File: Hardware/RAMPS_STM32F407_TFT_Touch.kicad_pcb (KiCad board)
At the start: 2 copper layers, 110 x 83.7 mm, 99 parts, among them J1 TEMP_0, J10 FAN2, J11 FAN1, J12 X_logic, J13 Microsteps, J14 X-, J15 Y-, J16 Z-, J17 Left, J18 Y_logic, J19 X+, J2 TEMP_1, J20 Y+, J21 Z+, J22 Microsteps, J23 LCD2, J24 Z_logic, J25 TFT_FSCM, J26 Microsteps, J27 LCD1, J28 E0_logic, J29 Microsteps, J3 TEMP_B, J30 Right, J31 E1_logic, J32 Microsteps, J33 X_motor, J34 Y_motor, J35 Z_motor, J36 E0_motor, J37 E1_motor, J38 X, J39 Y, J4 TEMP_C, J40 Z, J41 E0, J42 E1, J43 FAN0, J44 COM, J45 USB, J46 Power, J47 I2C, J48 SPI, J49 SPI, J5 -VIN+, J50 SDIO, J51 Servo, J52 Servo, J53 PowerSelect, J54 Power, J56 Power, J6 HEATER_B, J7 HEATER_0, J8 HEATER_1, J9 FAN3, Q1 NTMFS5C628, Q2 NTMFS5C628, Q3 NTMFS5C628, Q4 BUK9K17-60E, Q5 BUK9K17-60E, U1 74LVC125, X01 MP2315, X02 MP2315

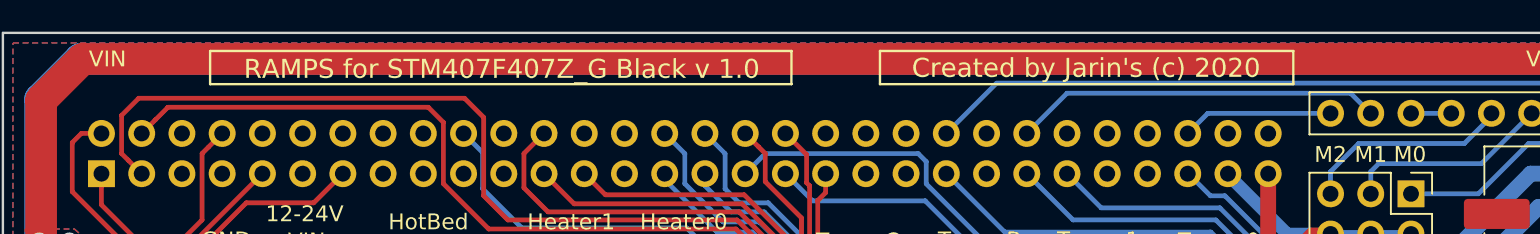
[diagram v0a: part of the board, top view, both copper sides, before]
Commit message: Added KiCADlibrary and 3Dshapes
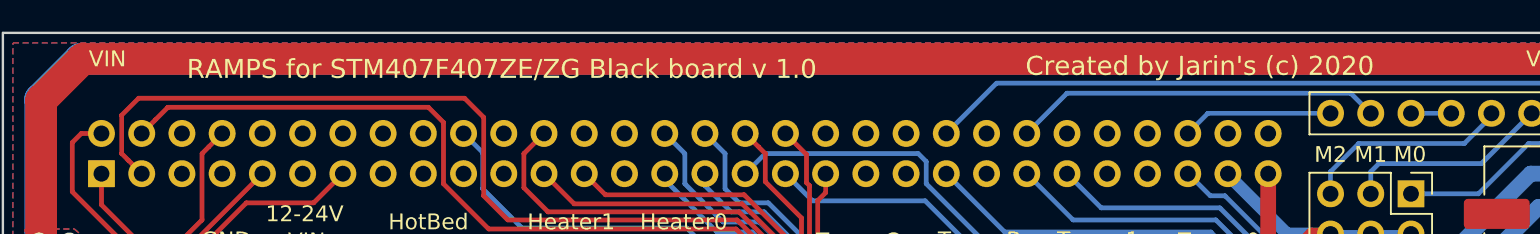
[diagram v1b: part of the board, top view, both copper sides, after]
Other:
- board text added: "RAMPS for STM407F407ZE/ZG Black board v 1.0"
- board text removed: "RAMPS for STM407F407Z_G Black v 1.0"
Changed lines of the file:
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@@
   (general
     (thickness 1.6)
-    (drawings 236)
+    (drawings 228)
     (tracks 1220)
     (zones 0)
@@
     (34 B.Paste user hide)
     (35 F.Paste user hide)
-    (36 B.SilkS user hide)
-    (37 F.SilkS user)
+    (36 B.SilkS user)
+    (37 F.SilkS user hide)
     (38 B.Mask user hide)
     (39 F.Mask user hide)
@@
   )
   (setup
-    (last_trace_width 1)
+    (last_trace_width 0.3)
     (user_trace_width 0.3)
     (user_trace_width 0.35)
@@
     (effects (font (size 0.8 0.8) (thickness 0.15)) (justify mirror))
   )
-  (gr_line (start 81.4705 1.143) (end 55.372 1.143) (layer F.SilkS) (width 0.15))
-  (gr_line (start 55.372 3.2385) (end 81.4705 3.2385) (layer F.SilkS) (width 0.15))
-  (gr_line (start 81.4705 3.2385) (end 81.4705 1.143) (layer F.SilkS) (width 0.15))
-  (gr_line (start 55.372 1.143) (end 55.372 3.2385) (layer F.SilkS) (width 0.15))
-  (gr_line (start 13.081 3.2385) (end 49.784 3.2385) (layer F.SilkS) (width 0.15))
-  (gr_line (start 13.081 1.143) (end 13.081 3.2385) (layer F.SilkS) (width 0.15))
-  (gr_line (start 49.784 1.143) (end 13.081 1.143) (layer F.SilkS) (width 0.15))
-  (gr_line (start 49.784 3.2385) (end 49.784 1.143) (layer F.SilkS) (width 0.15))
   (gr_text "Power supply for \nexternal use" (at 38.9255 52.578) (layer F.SilkS)
     (effects (font (size 0.8 0.8) (thickness 0.12)))
@@
     (effects (font (size 1 1) (thickness 0.15)))
   )
-  (gr_text "Created by Jarin's (c) 2020" (at 68.3895 2.2225) (layer F.SilkS)
+  (gr_text "Created by Jarin's (c) 2020" (at 75.565 2.0955) (layer F.SilkS)
     (effects (font (size 1.2 1.2) (thickness 0.15)))
   )
-  (gr_text "RAMPS for STM407F407Z_G Black v 1.0" (at 31.496 2.286) (layer F.SilkS)
+  (gr_text "RAMPS for STM407F407ZE/ZG Black board v 1.0" (at 31.496 2.286) (layer F.SilkS)
     (effects (font (size 1.2 1.2) (thickness 0.15)))
   )
@@
     (effects (font (size 1 1) (thickness 0.15)) (justify mirror))
   )
-  (gr_text "Created by Jarin's (c) 2020" (at 19.4945 71.12) (layer B.SilkS)
+  (gr_text "Created by Jarin's (c) 2020" (at 14.2875 71.5645) (layer B.SilkS)
     (effects (font (size 1.2 1.2) (thickness 0.15)) (justify mirror))
   )
-  (gr_text "RAMPS for STM407F407Z_G Black v 1.0" (at 20.193 68.834) (layer B.SilkS)
+  (gr_text "RAMPS for STM407F407ZE/ZG Black board v 1.0" (at 23.8125 69.1515) (layer B.SilkS)
     (effects (font (size 1.2 1.2) (thickness 0.15)) (justify mirror))
   )
@@
   (gr_poly (pts (xy 136.5 115.6) (xy 142.9 115.6) (xy 142.9 121.4) (xy 136.5 121.4)) (layer B.Mask) (width 0.15))
   (gr_poly (pts (xy 136.525 113.665) (xy 136.525 102.87) (xy 146.05 102.87) (xy 146.05 113.665)) (layer B.Mask) (width 0.15))
-  (via (at 40.386 68.8975) (size 0.8) (drill 0.4) (layers F.Cu B.Cu) (net 7))
   (segment (start 47.839 61.8725) (end 46.228 61.8725) (width 1.5) (layer F.Cu) (net 1))
   (segment (start 49.4665 68.8975) (end 49.4665 63.5) (width 1.5) (layer F.Cu) (net 1))
@@
   (segment (start 34.5865 34.5625) (end 34.5865 28.088) (width 0.3) (layer F.Cu) (net 6))
   (segment (start 34.5865 28.088) (end 35.179 27.4955) (width 0.3) (layer F.Cu) (net 6))
+  (via (at 40.386 68.8975) (size 0.8) (drill 0.4) (layers F.Cu B.Cu) (net 7))
   (segment (start 28.0975 68.9025) (end 27.813 68.618) (width 0.3) (layer F.Cu) (net 7))
   (segment (start 27.846 68.9025) (end 27.813 68.9355) (width 0.5) (layer F.Cu) (net 7))

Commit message: Add Gerber files
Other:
- board text added: "VIN - 24V"
- board text removed: "CS1"
- board text removed: "CS2"

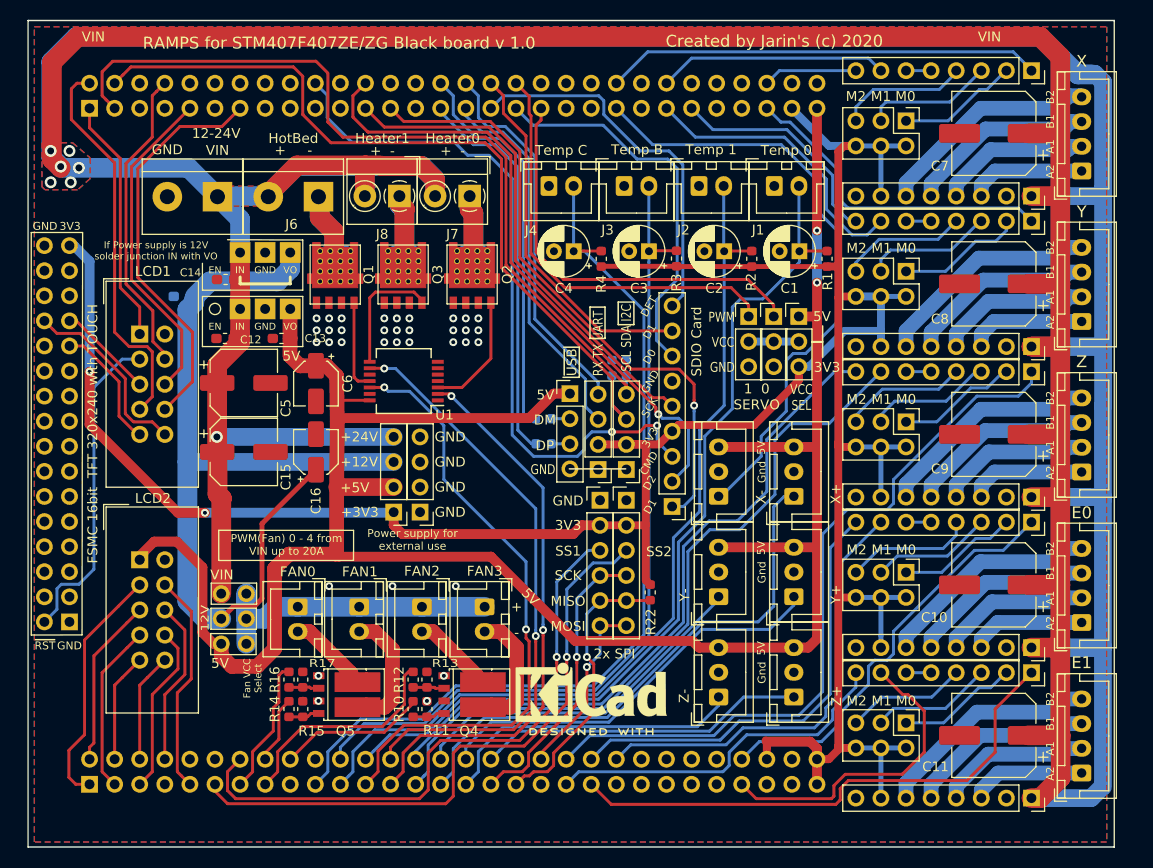
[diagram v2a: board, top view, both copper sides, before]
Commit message: Add fuse
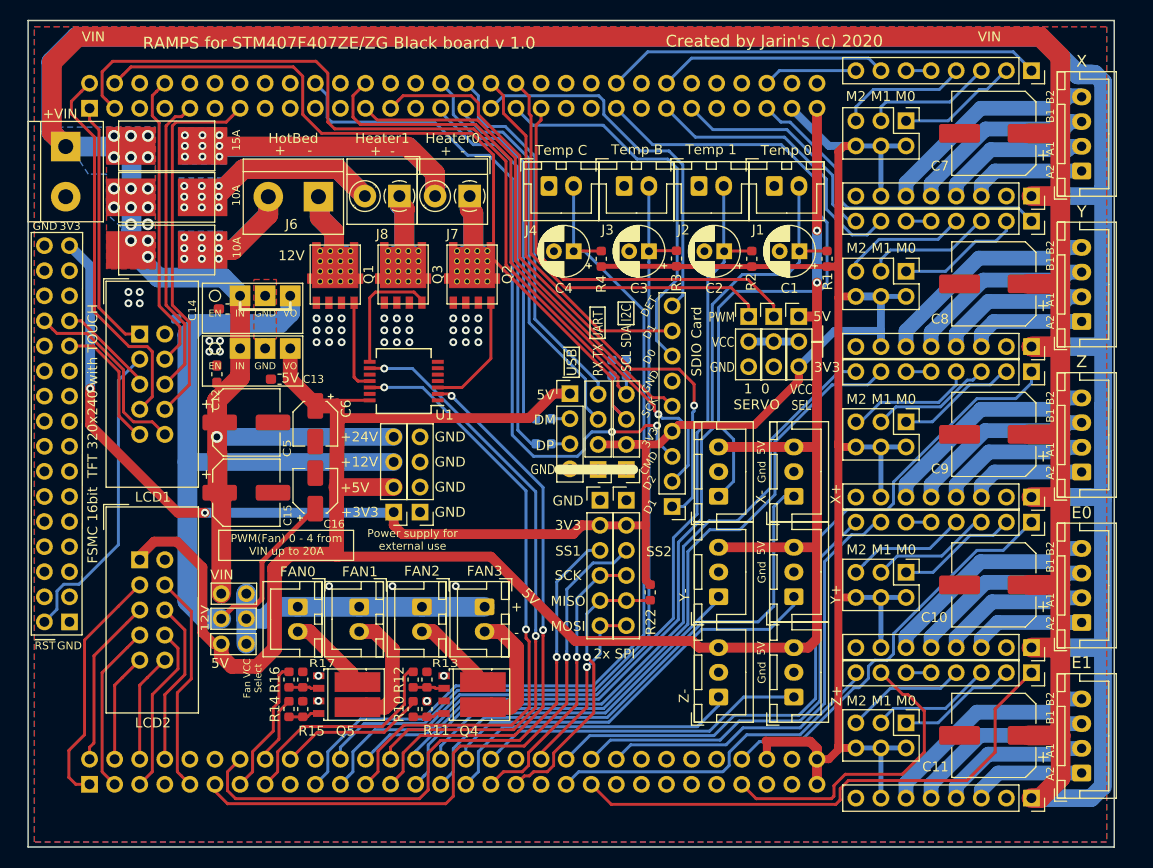
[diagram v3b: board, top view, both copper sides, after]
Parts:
- removed REF**: KiCad-Logo2_6mm_SilkScreen, Symbol:KiCad-Logo2_6mm_SilkScreen
- removed REF**: KiCad-Logo2_8mm_SilkScreen, Symbol:KiCad-Logo2_8mm_SilkScreen
- added F1: 15A, Jarin's:2410_FuseFolder, F.Cu at (14.0, 12.7)
- added F2: 10A, Jarin's:2410_FuseFolder, F.Cu at (14.0, 17.9)
- added F3: 10A, Jarin's:2410_FuseFolder, F.Cu at (14.0, 23.2)
- moved J5 16.2 mm to (3.81, 12.8), turned to 270 degrees
- moved X02 4.38 mm to (21.5, 27.9)
- moved C15 4.14 mm to (22.1, 47.8)
- moved C13 4.13 mm to (25.5, 36.3)
- moved C6 4.06 mm to (29.1, 40.8)
- moved C5 4.01 mm to (22.1, 40.7)
- moved X01 4.00 mm to (21.5, 33.2)
- moved C16 3.94 mm to (29.1, 47.6)
- moved C12 3.71 mm to (19.1, 35.8), turned to 90 degrees
- moved C14 2.99 mm to (20.2, 29.2)
- moved C17 2.30 mm to (15.9, 30.2)
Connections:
- J6 pad 2: +24V -> Net-(F3-Pad2)
- J7 pad 2: +24V -> Net-(F1-Pad2)
- J8 pad 2: +24V -> Net-(F2-Pad2)
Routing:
- net Net-(F1-Pad2): track 0.00 -> 53.0 mm, vias 0 -> 9
- net +24V: track 604.0 -> 553.2 mm, vias 7 -> 18
- net Net-(F2-Pad2): track 0.00 -> 36.4 mm, vias 0 -> 9
- net Net-(F3-Pad2): track 0.00 -> 19.9 mm, vias 0 -> 9
- net +12V: track 88.8 -> 81.4 mm
- net /X_MIN: track 62.1 -> 66.6 mm
- net +5V: track 232.4 -> 229.1 mm
- net /EN1: track 40.7 -> 38.0 mm
- net /EN2: track 33.2 -> 30.9 mm
- net /SDIO_D2: track 62.6 -> 64.0 mm
- net /TEMP_0: track 90.7 -> 92.0 mm
- net /~RESET: track 32.7 -> 31.5 mm
- net /E0_EN: track 42.3 -> 41.2 mm
- net /E1_DIR: track 36.2 -> 35.2 mm
- net /HEATER_B: track 62.3 -> 63.3 mm
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- added copper zone on B.Cu, net Net-(F1-Pad2)
- added copper zone on B.Cu, net Net-(F2-Pad2)
- added copper zone on B.Cu, net Net-(F3-Pad2)
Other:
- board text added: "+VIN"
- board text removed: "12-24V"
- board text removed: "If Power supply is 12V solder junction IN with VO"

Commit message: Add Schottky to 5V(usb port protection)
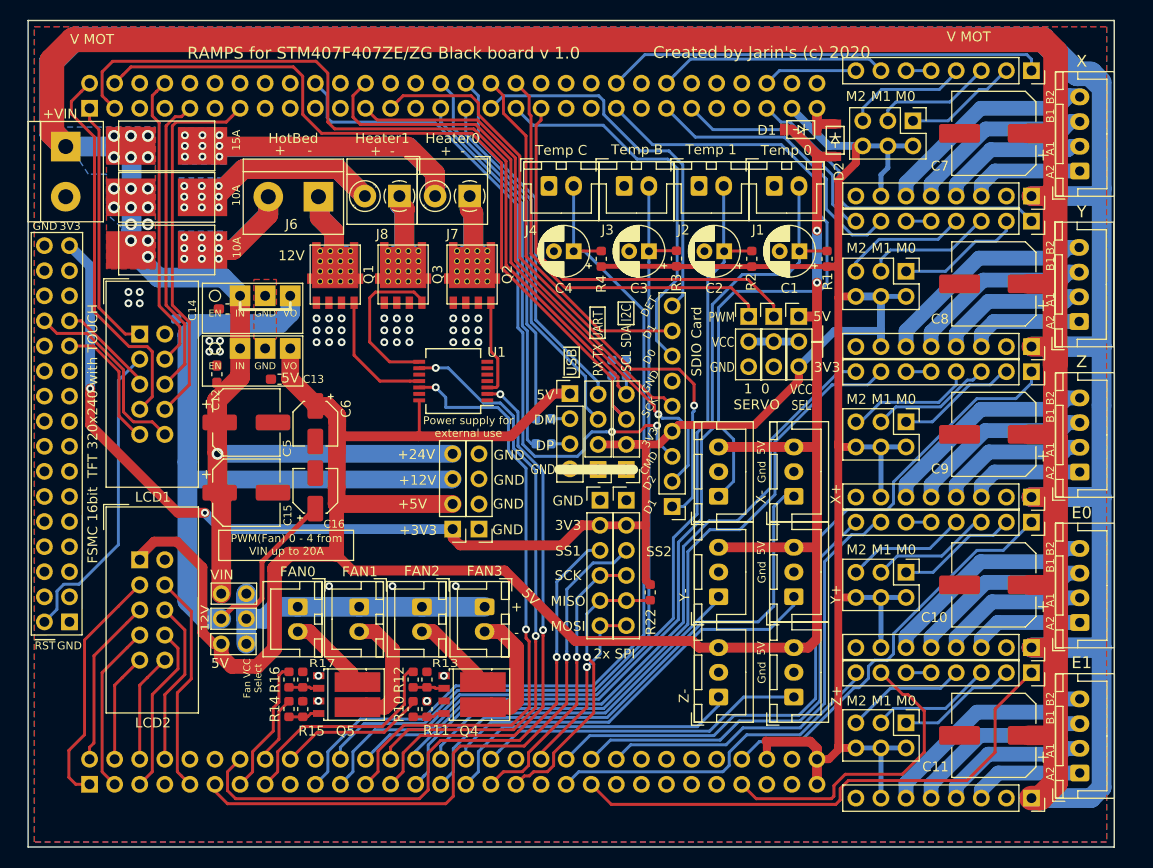
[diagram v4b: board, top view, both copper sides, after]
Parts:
- added D1: MBR130LSFT1G, Jarin's:D_SOD-123, F.Cu at (78.2, 11.0)
- added D2: MBR130LSFT1G, Jarin's:D_SOD-123, F.Cu at (81.7, 12.1)
- moved J46 6.21 mm to (45.7, 51.5)
- moved J54 6.21 mm to (43.0, 51.5)
- moved U1 5.02 mm to (43.1, 36.5)
- moved J13 0.70 mm to (89.6, 10.2)
- moved J39 0.25 mm to (106.4, 30.5)
- moved J38 0.19 mm to (106.5, 15.2)
- moved J40 0.19 mm to (106.5, 45.7)
- moved J41 0.19 mm to (106.5, 61.0)
- moved J42 0.19 mm to (106.5, 76.2)
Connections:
- J17 pad 59: +5V -> Net-(D1-Pad1)
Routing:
- net +5V: track 229.1 -> 238.5 mm
- net +12V: track 81.4 -> 89.2 mm
- net Net-(D1-Pad1): track 0.00 -> 3.99 mm
- net Net-(Q3-Pad1): track 12.3 -> 16.2 mm
- net Net-(Q1-Pad1): track 9.28 -> 13.0 mm
- net Net-(Q2-Pad1): track 12.2 -> 9.84 mm
- net /HEATER_0: track 56.6 -> 54.7 mm
- net /USB_DM: track 39.9 -> 38.0 mm
- net /HEATER_1: track 61.4 -> 59.6 mm
- net /SDIO_CMD: track 72.4 -> 71.1 mm
- net /USB_DP: track 39.5 -> 38.2 mm
- net /RX: track 38.3 -> 37.0 mm
- net /HEATER_B: track 63.3 -> 62.1 mm
- net /TX: track 38.1 -> 37.0 mm
- net +3V3: track 299.5 -> 300.4 mm
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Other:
- board text added: "V MOT"

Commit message: .
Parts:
- C1, C2, C3, C4: footprint Capacitor_THT:CP_Radial_D5.0mm_P2.00mm -> Capacitor_SMD:CP_Elec_4x5.3
- C10, C11, C7, C8, C9: footprint Capacitor_SMD:CP_Elec_8x6.9 -> Capacitor_SMD:CP_Elec_6.3x5.8
- moved J6 1.91 mm to (29.4, 19.7)
- moved Q1 1.91 mm to (29.2, 30.5)
- moved Q2 1.91 mm to (43.1, 30.5)
- moved Q3 1.91 mm to (36.1, 30.5)
- moved J7 1.90 mm to (44.7, 19.7)
- moved J8 1.90 mm to (37.6, 19.7)
- moved U1 1.90 mm to (43.1, 38.4)
- moved C1 1.89 mm to (76.3, 22.7)
- moved C2 1.31 mm to (69.3, 22.7)
- moved R4 1.04 mm to (58.7, 25.0)
- moved R2 0.97 mm to (72.8, 25.0)
- moved C3 0.90 mm to (62.2, 22.7)
- moved R3 0.86 mm to (65.8, 25.0)
- moved C4 0.64 mm to (55.2, 22.7)
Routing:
- net Net-(J7-Pad1): track 25.3 -> 18.0 mm
- net Net-(J6-Pad1): track 26.2 -> 19.4 mm
- net Net-(J8-Pad1): track 22.7 -> 17.1 mm
- net +24V: track 553.5 -> 557.4 mm
- net Net-(F3-Pad2): track 19.9 -> 16.6 mm
- net Net-(F2-Pad2): track 36.4 -> 38.7 mm
- net Net-(F1-Pad2): track 53.0 -> 55.0 mm
- net +5V: track 238.5 -> 236.6 mm
- net /HEATER_B: track 62.1 -> 60.4 mm
- net /HEATER_1: track 59.6 -> 58.5 mm
- net /HEATER_0: track 54.7 -> 53.6 mm
- net /TEMP_C: track 92.6 -> 91.5 mm, vias 0 -> 1
- net Net-(Q3-Pad1): track 16.2 -> 17.0 mm
- net /SERVO0: track 42.2 -> 42.8 mm
- net /TEMP_1: track 90.6 -> 90.1 mm, vias 0 -> 1
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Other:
- board text removed: "PWM(Fan) 0 - 4 from VIN up to 20A"

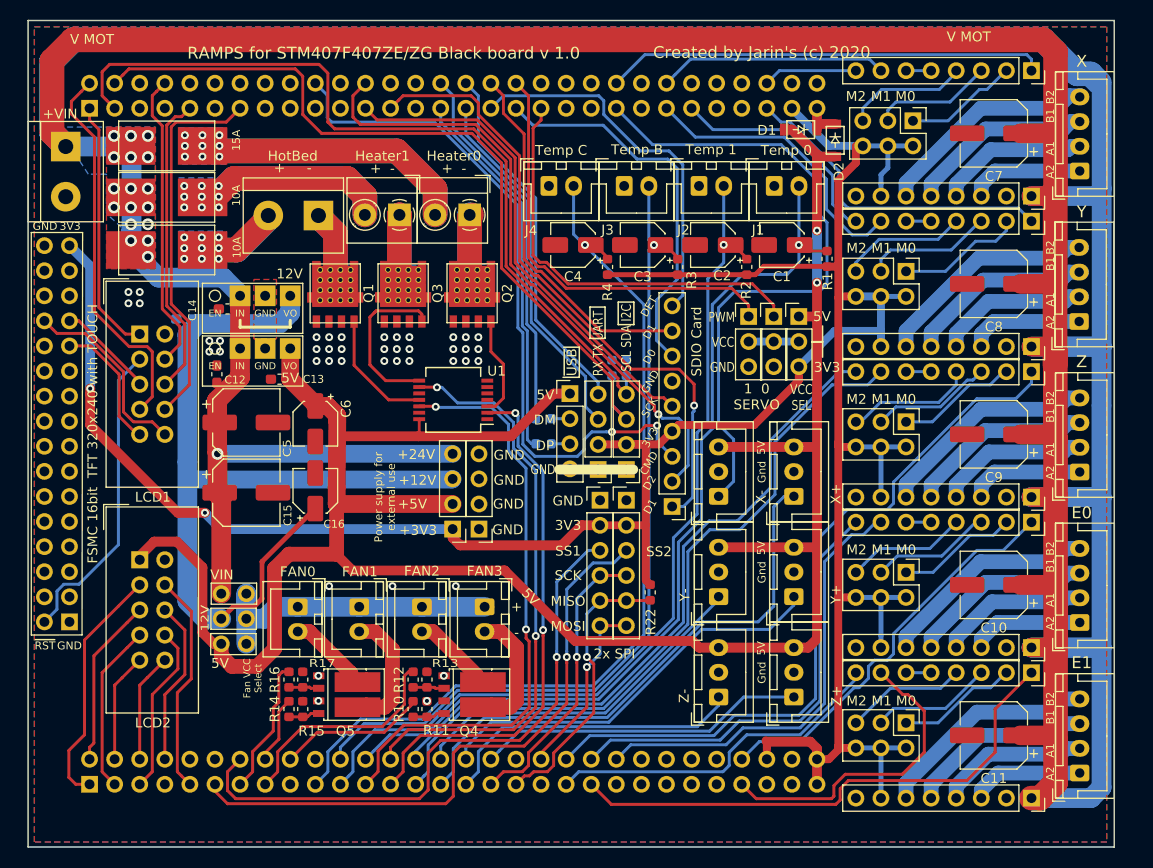
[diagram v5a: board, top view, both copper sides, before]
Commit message: Correct the placement of the connectors in the correct position
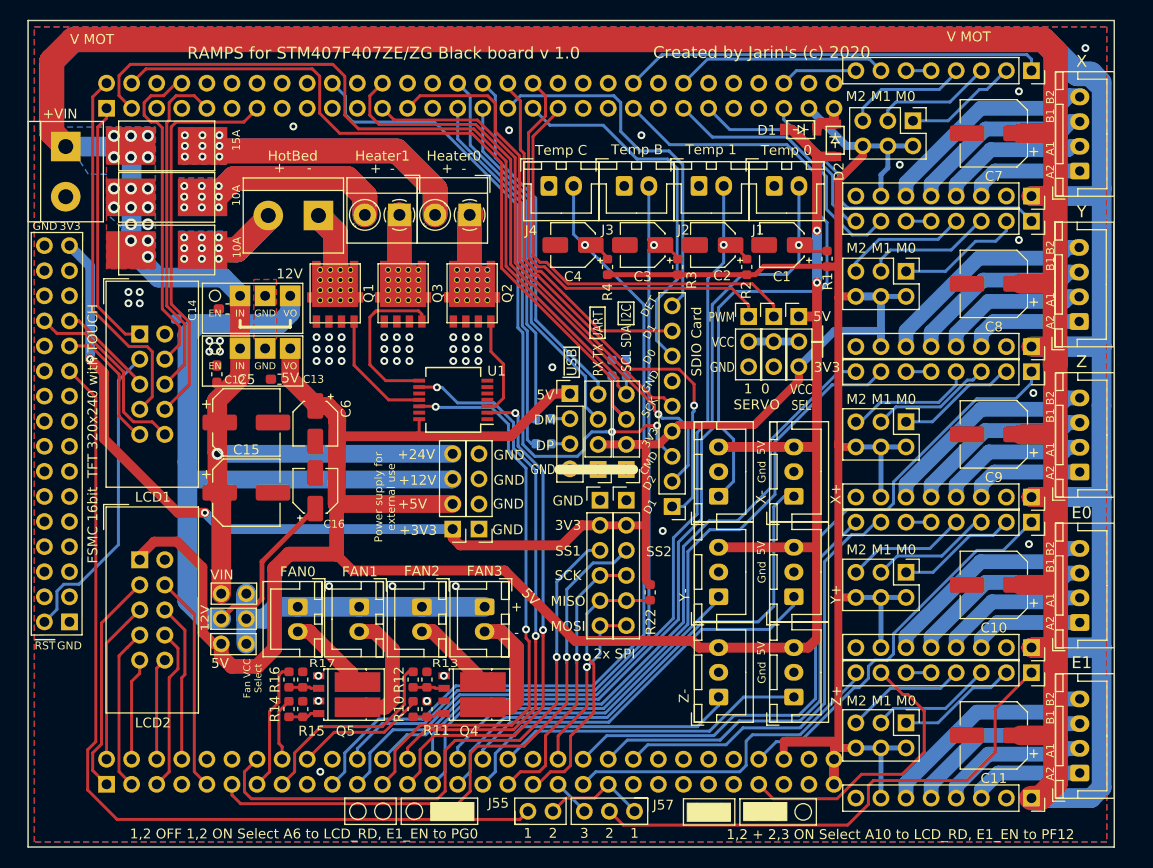
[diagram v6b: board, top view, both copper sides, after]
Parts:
- added J55: Conn_01x02, Connector_PinHeader_2.54mm:PinHeader_1x02_P2.54mm_Vertical, F.Cu at (50.6, 80.1)
- added J57: LCD RS Select, Connector_PinHeader_2.54mm:PinHeader_1x03_P2.54mm_Vertical, F.Cu at (61.4, 80.1)
- C15, C5: footprint Capacitor_SMD:CP_Elec_6.3x7.7 -> Capacitor_SMD:CP_Elec_6.3x5.8
- moved J17 1.72 mm to (7.94, 8.89)
- moved J30 1.72 mm to (7.94, 77.3)
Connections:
- J25 pad 21: (no net) -> Net-(J25-Pad21)
- J30 pad 37: (no net) -> Net-(J30-Pad37)
- J30 pad 41: /E1_EN -> Net-(J30-Pad41)
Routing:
- net Net-(J25-Pad21): track 0.00 -> 90.0 mm
- net Net-(J30-Pad41): track 0.00 -> 10.6 mm
- net /EN2: track 30.9 -> 34.8 mm
- net Net-(J30-Pad37): track 0.00 -> 3.83 mm
- net +3V3: track 300.3 -> 296.9 mm
- net /SDDET: track 30.3 -> 33.1 mm
- net /SDA: track 82.9 -> 80.4 mm
- net /E1_STEP: track 31.8 -> 29.5 mm
- net /LCD7: track 24.9 -> 22.7 mm
- net /SDIO_CMD: track 71.1 -> 69.1 mm
- net /X_MAX: track 55.1 -> 53.2 mm
- net /Y_MAX: track 41.2 -> 39.4 mm
- net /Z_MIN: track 30.9 -> 29.1 mm
- net /SS2: track 62.8 -> 61.0 mm
- net /SDIO_D3: track 63.5 -> 61.7 mm
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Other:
- board text added: "1"
- board text added: "1,2 + 2,3 ON Select A10 to LCD_RD, E1_EN to PF12"
- board text added: "1,2 OFF 1,2 ON Select A6 to LCD_RD, E1_EN to PG0"
- board text added: "2"
- board text added: "3"
